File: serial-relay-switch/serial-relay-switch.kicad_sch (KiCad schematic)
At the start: 76 parts, among them J1 Screw_Terminal_01x01, J10 Screw_Terminal_01x01, J11 Screw_Terminal_01x01, J17 Conn_01x01, J18 Conn_01x01, J19 Screw_Terminal_01x01, J2 2501551-4, J20 Screw_Terminal_01x01, J21 Conn_01x01, J4 Screw_Terminal_01x01, J5 Screw_Terminal_01x01, J6 Screw_Terminal_01x01, J7 Screw_Terminal_01x01, J8 Screw_Terminal_01x01, J9 Screw_Terminal_01x01, K1 G2RL-1-E, K2 G2RL-1-E, K3 G2RL-1-E, K4 G2RL-1-E, K5 G2RL-1-E, K6 G2RL-1-E, K7 G2RL-1-E, K8 G2RL-1-E, U1 H11L1, U13 STM1810T, U14 74LVC1G32, U15 74LVC1G08, U16 74LVC1G04, U17 74LS163, U2 ISL8488E, U3 SZNUD3124DMT1G, U4 ISL8488E, U5 74HC594, U6 SZNUD3124DMT1G, U7 SZNUD3124DMT1G, U8 SZNUD3124DMT1G

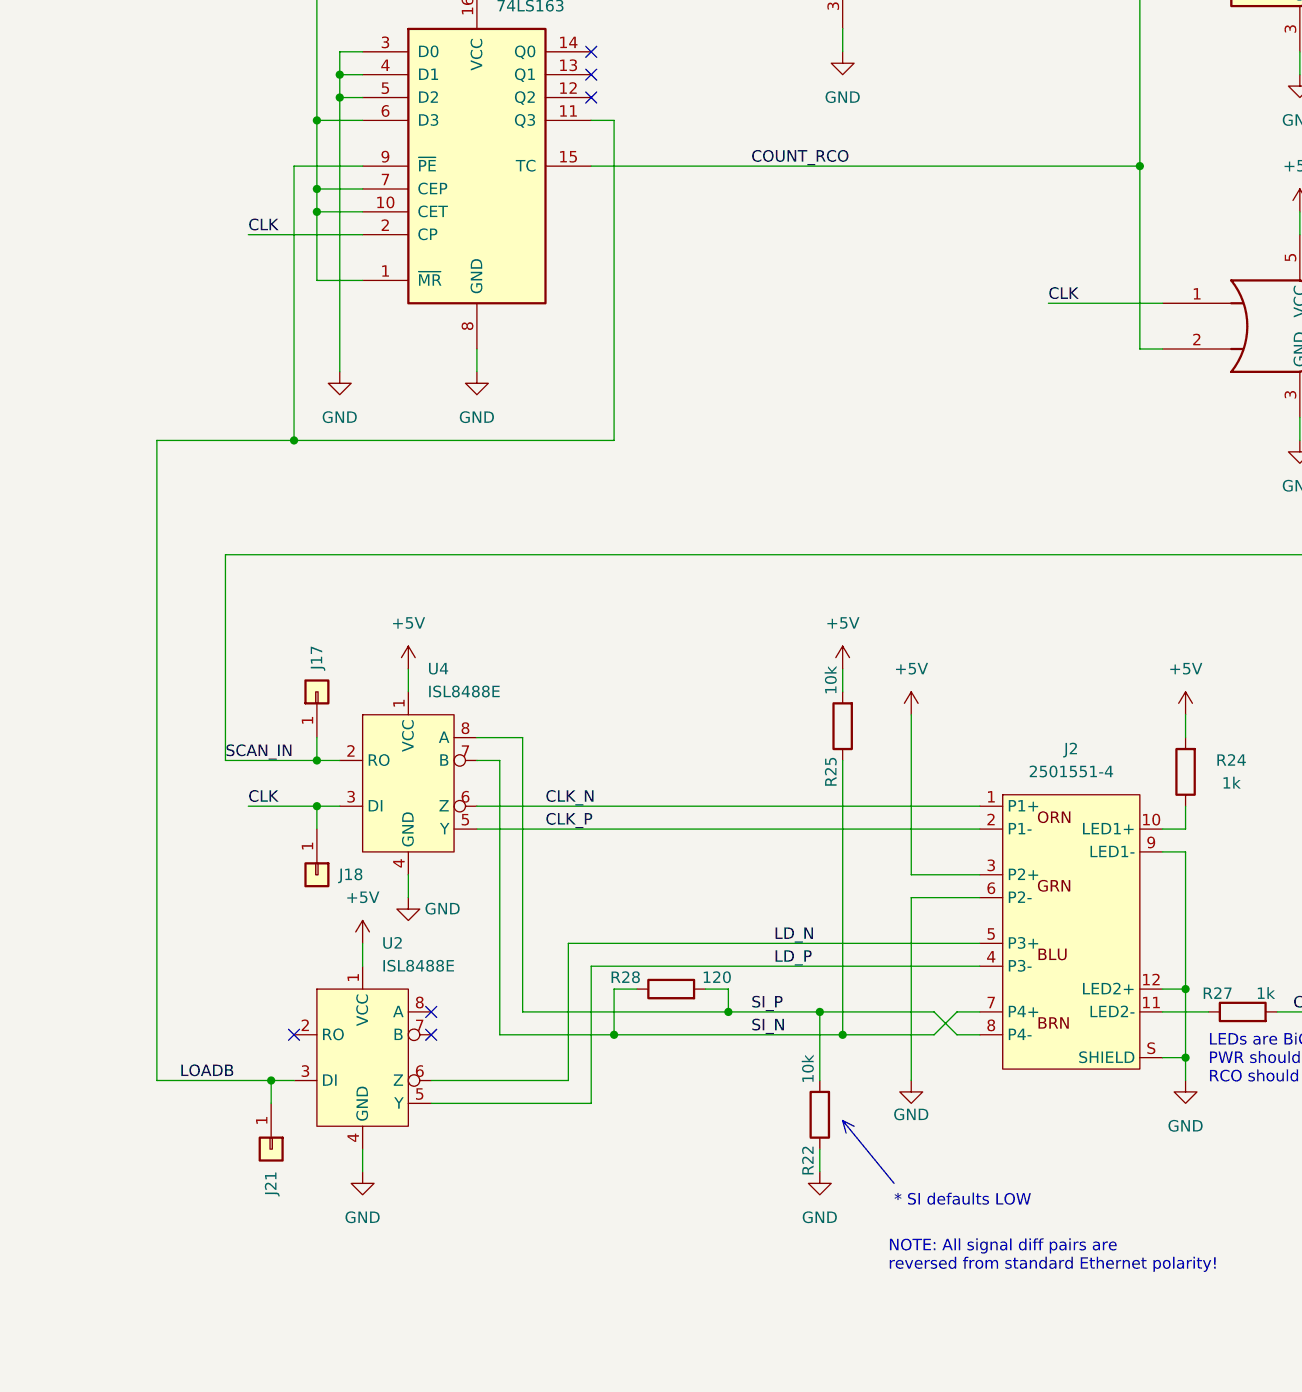
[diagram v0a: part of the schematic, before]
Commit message: [rs] Correct timing in LOADB signal
Moved the LOAD signal to be from the counter's
RCO instead of the MSb of the count. This moves
the load pulse one clock cycle earlier and corrects
an off-by-one error in the receive shift register
timing, causing relay H to not be controllable
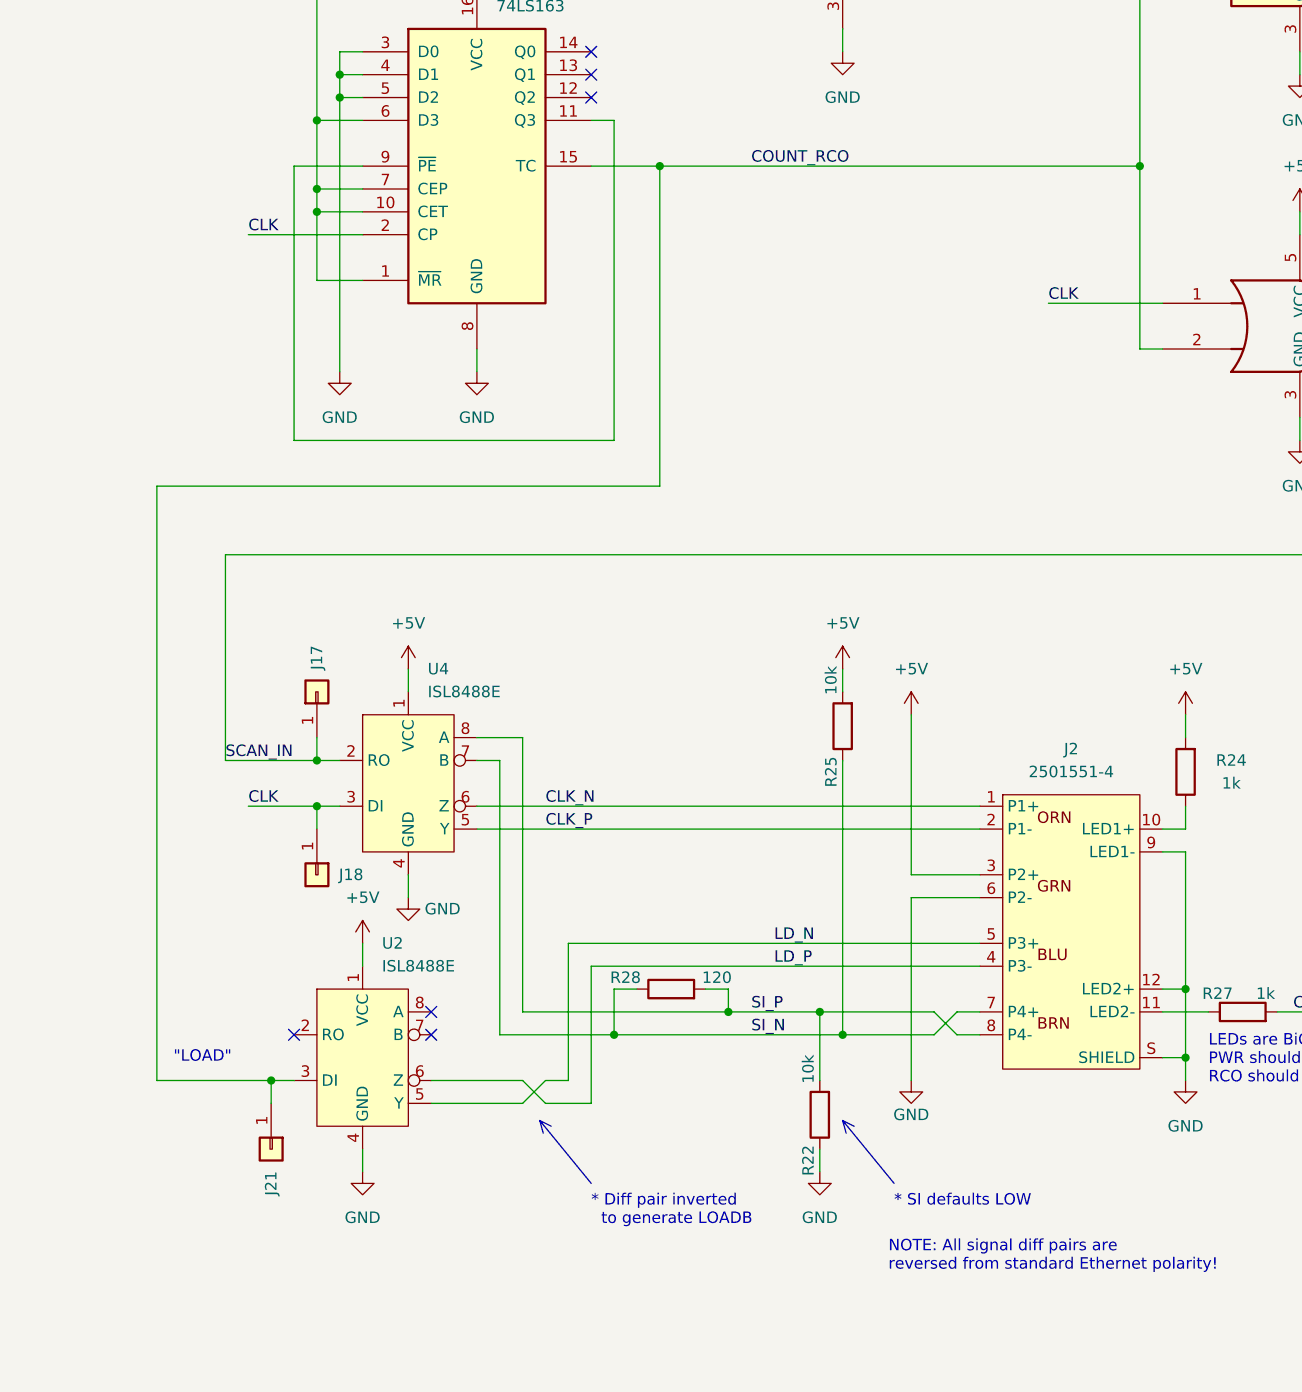
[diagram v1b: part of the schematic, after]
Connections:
- net COUNT_RCO: now also J21.1 (Pin_1), U2.3 (DI)
- net LD_N: now also U2.5 (Y); no longer U2.6 (Z)
- net LD_P: now also U2.6 (Z); no longer U2.5 (Y)
- net LOADB: no longer names the net of U17.11 (Q3), U17.9 (~{PE})
- net LOADB: no longer J21.1 (Pin_1), U2.3 (DI)
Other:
- note added: ""LOAD""
- note added: "* Diff pair inverted to generate LOADB"
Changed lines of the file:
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@@
 		)
 	)
+	(text "\"LOAD\""
+		(exclude_from_sim no)
+		(at 33.02 233.68 0)
+		(effects
+			(font
+				(size 1.27 1.27)
+			)
+		)
+	)
 	(text "'166 internal count"
 		(exclude_from_sim no)
@@
 		)
 	)
+	(text "* Diff pair inverted\n  to generate LOADB"
+		(exclude_from_sim no)
+		(at 76.2 248.92 0)
+		(effects
+			(font
+				(size 1.27 1.27)
+			)
+			(justify left top)
+		)
+	)
 	(text "* SI defaults LOW"
 		(exclude_from_sim no)
@@
 	)
 	(junction
-		(at 43.18 165.1)
-		(diameter 0)
-		(color 0 0 0 0)
-	)
-	(junction
 		(at 271.78 149.86)
 		(diameter 0)
@@
 	)
 	(junction
+		(at 83.82 134.62)
+		(diameter 0)
+		(color 0 0 0 0)
+	)
+	(junction
 		(at 391.16 144.78)
 		(diameter 0)
@@
 	(wire
 		(pts
+			(xy 58.42 238.76) (xy 68.58 238.76)
+		)
+		(stroke
+			(width 0)
+			(type default)
+		)
+	)
+	(wire
+		(pts
 			(xy 297.18 73.66) (xy 297.18 76.2)
 		)
@@
 	(wire
 		(pts
+			(xy 27.94 170.18) (xy 27.94 236.22)
+		)
+		(stroke
+			(width 0)
+			(type default)
+		)
+	)
+	(wire
+		(pts
 			(xy 317.5 144.78) (xy 327.66 144.78)
 		)
@@
 	(wire
 		(pts
-			(xy 142.24 233.68) (xy 142.24 236.22)
+			(xy 83.82 134.62) (xy 137.16 134.62)
 		)
 		(stroke
@@
 	(wire
 		(pts
-			(xy 284.48 124.46) (xy 287.02 124.46)
+			(xy 142.24 233.68) (xy 142.24 236.22)
 		)
 		(stroke
@@
 	(wire
 		(pts
-			(xy 38.1 53.34) (xy 38.1 33.02)
+			(xy 284.48 124.46) (xy 287.02 124.46)
 		)
 		(stroke
@@
 	(wire
 		(pts
-			(xy 58.42 238.76) (xy 76.2 238.76)
+			(xy 38.1 53.34) (xy 38.1 33.02)
 		)
 		(stroke
@@
 	(wire
 		(pts
+			(xy 58.42 236.22) (xy 68.58 236.22)
+		)
+		(stroke
+			(width 0)
+			(type default)
+		)
+	)
+	(wire
+		(pts
 			(xy 370.84 106.68) (xy 370.84 109.22)
 		)
@@
 		)
 	)
+	(polyline
+		(pts
+			(xy 70.485 240.665) (xy 71.755 241.3)
+		)
+		(stroke
+			(width 0)
+			(type default)
+		)
+	)
 	(wire
 		(pts
@@
 	(wire
 		(pts
-			(xy 76.2 134.62) (xy 137.16 134.62)
+			(xy 76.2 134.62) (xy 83.82 134.62)
 		)
 		(stroke
@@
 	(wire
 		(pts
-			(xy 58.42 236.22) (xy 73.66 236.22)
-		)
-		(stroke
-			(width 0)
-			(type default)
-		)
-	)
-	(wire
-		(pts
 			(xy 271.78 119.38) (xy 363.22 119.38)
 		)
@@
 		)
 	)
+	(polyline
+		(pts
+			(xy 76.2 247.65) (xy 70.485 240.665)
+		)
+		(stroke
+			(width 0)
+			(type default)
+		)
+	)
 	(wire
 		(pts
@@
 	(wire
 		(pts
-			(xy 104.14 55.88) (xy 104.14 58.42)
+			(xy 83.82 134.62) (xy 83.82 170.18)
 		)
 		(stroke
@@
 	(wire
 		(pts
-			(xy 35.56 48.26) (xy 35.56 66.04)
+			(xy 104.14 55.88) (xy 104.14 58.42)
 		)
 		(stroke
@@
 	(wire
 		(pts
-			(xy 391.16 73.66) (xy 391.16 96.52)
+			(xy 35.56 48.26) (xy 35.56 66.04)
 		)
 		(stroke
@@
 	(wire
 		(pts
-			(xy 154.94 121.92) (xy 154.94 124.46)
+			(xy 391.16 73.66) (xy 391.16 96.52)
 		)
 		(stroke
@@
 	(wire
 		(pts
-			(xy 53.34 58.42) (xy 55.88 58.42)
+			(xy 154.94 121.92) (xy 154.94 124.46)
 		)
 		(stroke
@@
 	(wire
 		(pts
-			(xy 317.5 93.98) (xy 317.5 96.52)
+			(xy 53.34 58.42) (xy 55.88 58.42)
 		)
 		(stroke
@@
 	(wire
 		(pts
-			(xy 276.86 170.18) (xy 271.78 170.18)
+			(xy 317.5 93.98) (xy 317.5 96.52)
 		)
 		(stroke
@@
 	(wire
 		(pts
-			(xy 81.28 109.22) (xy 93.98 109.22)
+			(xy 276.86 170.18) (xy 271.78 170.18)
 		)
 		(stroke
@@
 	(wire
 		(pts
-			(xy 27.94 165.1) (xy 43.18 165.1)
+			(xy 81.28 109.22) (xy 93.98 109.22)
 		)
 		(stroke
@@
 	(wire
 		(pts
+			(xy 73.66 236.22) (xy 71.12 236.22)
+		)
+		(stroke
+			(width 0)
+			(type default)
+		)
+	)
+	(wire
+		(pts
 			(xy 383.54 172.72) (xy 393.7 172.72)
 		)
@@
 	(wire
 		(pts
+			(xy 71.12 236.22) (xy 68.58 238.76)
+		)
+		(stroke
+			(width 0)
+			(type default)
+		)
+	)
+	(wire
+		(pts
 			(xy 363.22 198.12) (xy 365.76 198.12)
 		)
@@
 	(wire
 		(pts
+			(xy 83.82 170.18) (xy 27.94 170.18)
+		)
+		(stroke
+			(width 0)
+			(type default)
+		)
+	)
+	(wire
+		(pts
+			(xy 71.12 238.76) (xy 76.2 238.76)
+		)
+		(stroke
+			(width 0)
+			(type default)
+		)
+	)
+	(wire
+		(pts
 			(xy 383.54 127) (xy 383.54 124.46)
 		)
@@
 		)
 	)
+	(polyline
+		(pts
+			(xy 70.485 240.665) (xy 70.866 242.062)
+		)
+		(stroke
+			(width 0)
+			(type default)
+		)
+	)
 	(wire
 		(pts
@@
 	(wire
 		(pts
-			(xy 27.94 236.22) (xy 27.94 165.1)
-		)
-		(stroke
-			(width 0)
-			(type default)
-		)
-	)
-	(wire
-		(pts
 			(xy 363.22 119.38) (xy 363.22 101.6)
 		)
@@
 	(wire
 		(pts
+			(xy 68.58 236.22) (xy 71.12 238.76)
+		)
+		(stroke
+			(width 0)
+			(type default)
+		)
+	)
+	(wire
+		(pts
 			(xy 213.36 119.38) (xy 215.9 119.38)
 		)
@@
 		(effects
 			(font
-				(size 1.27 1.27)
-			)
-			(justify left bottom)
-		)
-	)
-	(label "LOADB"
-		(at 30.48 236.22 0)
-		(effects
-			(font
